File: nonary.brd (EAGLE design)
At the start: 285.8 x 82.5 mm, 145 parts, among them J1 USB-C-12401598E4#2A

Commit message: Made modifications to the keyboard.lbr, brd, and sch files
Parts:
- removed D1, D10, D11, D12, D13, D14, D15, D16, D17, D18, D19, D2, D20, D21, D22, D23, D24, D25, D26, D27, D28, D29, D3, D30, D31, D32, D33, D34, D35, D36, D37, D38, D39, D4, D40, D41, D42, D43, D44, D45, D46, D47, D48, D49, D5, D50, D51, D52, D53, D54, D55, D56, D57, D58, D59, D6, D60, D61, D62, D8, D9: (no value), Components:DFN0603-2
- removed F1, F3, F4, F5, K_", K_,, K_-, K_., K_/, K_0, K_1, K_2, K_3, K_4, K_5, K_6, K_7, K_8, K_9, K_=, K_A, K_B, K_BACKSLASH, K_BACKSPACE, K_C, K_CAPSLOCK, K_D, K_E, K_ENTER, K_F, K_G, K_H, K_I, K_J, K_K, K_L, K_LALT, K_LCTRL, K_LSHIFT, K_LWIN, K_M, K_N, K_O, K_P, K_Q, K_R, K_RALT, K_RCTRL, K_RFN1, K_RFN2, K_RSHIFT, K_RWIN, K_S, K_SEMICOLON, K_SPACE, K_T, K_TAB, K_U, K_V, K_W, K_X, K_Y, K_Z, K_[, K_], K_`: KEYSWITCH-LEDTHTHOLE-MXHS-1U-LEDTHTHOLE, Keyboard:MXHS-1U-LEDTHTHOLE
- removed J1: USB-C-12401598E4#2A, USB:12401598E4#2A
- removed R4: 22, rcl:R0603
- added C10, C11, C9: 0.1uF, Components:C0603
- added C12, C13, C14: 0.47uF, Components:C0603
- added IC1: IS31FL3733-TQLS4, SamacSys_Parts:QFP50P900X900X120-49N
- added IC2: TLV75533PDBVR, SamacSys_Parts:SOT95P280X145-5N
- added J2: USB4065-XX-X_REVA, USB4065-XX-X_REVA:GCT_USB4065-XX-X_REVA
- added K1, K2, K3, K4, K5, K6, K7, K8, K9: KEYSWITCH-RGBSMDLED-MXHSPCB-1U-SMDRGB, Keyboard:MXHSPCB-1U-SMDRGB
- added Q1, Q2: BSS138, SamacSys_Parts:SOT95P240X120-3N
- added R10, R11, R8, R9: 10K, rcl:R0603
- added R5, R6: 5.1k, rcl:R0603
- added SV1: (no value), con-lstb:MA04-1
- C8: value 22pF -> 1uF
- D7: value (none) -> PRTR5V0U2X,215; device Components:DFN0603-2 -> SamacSys_Parts:SOT-143B
- F2: value KEYSWITCH-LEDTHTHOLE-MXHS-1U-LEDTHTHOLE -> MF-PSMF020X-2; device Keyboard:MXHS-1U-LEDTHTHOLE -> SamacSys_Parts:FUSC2214X85N
- R3: value 22 -> 10K
- moved D7 364.4 mm to (23.5, 88.0), turned to 270 degrees
- moved C1 242.4 mm to (3.56, 63.6)
- moved C7 239.3 mm to (18.7, 96.8), turned to 270 degrees
- moved C2 237.7 mm to (3.56, 66.2)
- moved C3 232.9 mm to (9.40, 96.8), turned to 270 degrees
- moved U$1 229.3 mm to (21.2, 69.0), turned to 270 degrees
- moved C4 225.9 mm to (11.7, 96.8), turned to 270 degrees
- moved C8 222.3 mm to (21.1, 96.8), turned to 270 degrees
- moved C5 219.0 mm to (14.0, 96.8), turned to 270 degrees
- moved R2 217.5 mm to (29.5, 63.1)
- moved X1 215.6 mm to (9.40, 69.1), turned to 90 degrees
- moved C6 212.0 mm to (16.3, 96.8), turned to 270 degrees
- moved R1 211.1 mm to (47.1, 88.6), turned to 90 degrees
- moved S1 190.6 mm to (51.8, 95.5)
- moved R3 187.0 mm to (60.5, 78.9)
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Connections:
- net N$1 renamed XTAL1
- net N$2 renamed XTAL2
- removed net COL0: F1.MX1, F2.MX1, F3.MX1, F4.MX1, F5.MX1, U$1.36
- removed net COL1: K_CAPSLOCK.MX1, K_LCTRL.MX1, K_LSHIFT.MX1, K_TAB.MX1, K_`.MX1
- removed net COL10: K_..MX1, K_9.MX1, K_L.MX1, K_O.MX1, K_RALT.MX1
- removed net COL12: K_/.MX1, K_0.MX1, K_P.MX1, K_RWIN.MX1, K_SEMICOLON.MX1
- removed net COL13: K_".MX1, K_-.MX1, K_RFN2.MX1, K_RSHIFT.MX1, K_[.MX1
- removed net COL14: K_BACKSLASH.MX1, K_BACKSPACE.MX1, K_ENTER.MX1, K_RCTRL.MX1, K_RFN1.MX1
- removed net COL2: K_1.MX1, K_A.MX1, K_LWIN.MX1, K_Q.MX1, K_Z.MX1
- removed net COL3: K_2.MX1, K_LALT.MX1, K_S.MX1, K_W.MX1, K_X.MX1
- removed net COL4: K_3.MX1, K_C.MX1, K_D.MX1, K_E.MX1
- removed net COL5: K_4.MX1, K_F.MX1, K_R.MX1, K_V.MX1
- removed net COL6: K_5.MX1, K_B.MX1, K_G.MX1, K_SPACE.MX1, K_T.MX1
- removed net COL7: K_6.MX1, K_H.MX1, K_N.MX1, K_Y.MX1
- removed net COL8: K_7.MX1, K_J.MX1, K_M.MX1, K_U.MX1
- removed net COL9: K_,.MX1, K_8.MX1, K_I.MX1, K_K.MX1
- removed net N$10: J1.A7, J1.B7, R4.2
- removed net N$11: D1.C, D2.A, K_`.MX2
- removed net N$12: D2.C, D3.A, K_1.MX2
- removed net N$14: D4.C, D5.A, K_3.MX2
- removed net N$15: D5.C, D6.A, K_4.MX2
- removed net N$16: D6.C, D7.A, K_5.MX2
- removed net N$17: D7.C, D8.A, K_6.MX2
- removed net N$18: D8.C, D9.A, K_7.MX2
- removed net N$20: D10.C, D11.A, K_9.MX2
- removed net N$21: D11.C, D12.A, K_0.MX2
- removed net N$22: D12.C, D13.A, K_-.MX2
- removed net N$23: D28.C, K_BACKSLASH.MX2
- removed net N$24: D13.C, D14.A, K_=.MX2
- removed net N$25: D14.C, K_BACKSPACE.MX2
- removed net N$28: D17.C, D18.A, K_W.MX2
- removed net N$29: D18.C, D19.A, K_E.MX2
- removed net N$30: D19.C, D20.A, K_R.MX2
- removed net N$31: D20.C, D21.A, K_T.MX2
- removed net N$32: D21.C, D22.A, K_Y.MX2
- removed net N$33: D22.C, D23.A, K_U.MX2
- removed net N$34: D23.C, D24.A, K_I.MX2
- removed net N$35: D24.C, D25.A, K_O.MX2
- removed net N$36: D25.C, D26.A, K_P.MX2
- removed net N$37: D26.C, D27.A, K_[.MX2
- removed net N$38: D34.C, D35.A, K_G.MX2
- removed net N$39: D27.C, D28.A, K_].MX2
- removed net N$40: D41.C, K_ENTER.MX2
- removed net N$41: D29.C, D30.A, K_CAPSLOCK.MX2
- removed net N$42: D30.C, D31.A, K_A.MX2
- removed net N$43: D31.C, D32.A, K_S.MX2
- removed net N$44: D32.C, D33.A, K_D.MX2
- removed net N$45: D33.C, D34.A, K_F.MX2
- removed net N$46: D40.C, D41.A, K_".MX2
- removed net N$47: D35.C, D36.A, K_H.MX2
- removed net N$48: D36.C, D37.A, K_J.MX2
- removed net N$49: D37.C, D38.A, K_K.MX2
- removed net N$50: D38.C, D39.A, K_L.MX2
- removed net N$51: D39.C, D40.A, K_SEMICOLON.MX2
- removed net N$52: D53.C, D54.A, K_RSHIFT.MX2
- removed net N$53: D54.C, K_RFN1.MX2
- removed net N$54: D47.C, D48.A, K_B.MX2
- removed net N$55: D60.C, D61.A, K_RWIN.MX2
- removed net N$56: D42.C, D43.A, K_LSHIFT.MX2
- removed net N$57: D43.C, D44.A, K_Z.MX2
- removed net N$58: D44.C, D45.A, K_X.MX2
- removed net N$59: D45.C, D46.A, K_C.MX2
- removed net N$6: J1.A4, J1.A9, J1.B4, J1.B9, U$1.2
- removed net N$60: D46.C, D47.A, K_V.MX2
- removed net N$61: K_=.MX1, K_].MX1
- removed net N$62: D48.C, D49.A, K_N.MX2
- removed net N$63: D49.C, D50.A, K_M.MX2
- removed net N$64: D50.C, D51.A, K_,.MX2
- removed net N$65: D51.C, D52.A, K_..MX2
- removed net N$66: D52.C, D53.A, K_/.MX2
- removed net N$7: J1.A6, J1.B6, R3.1
- removed net N$71: D55.C, D56.A, K_LCTRL.MX2
- removed net N$72: D56.C, D57.A, K_LWIN.MX2
- removed net N$73: D57.C, D58.A, K_LALT.MX2
- removed net N$74: D58.C, D59.A, K_SPACE.MX2
- removed net N$75: D59.C, D60.A, K_RALT.MX2
- removed net N$77: D61.C, D62.A, K_RFN2.MX2
- removed net N$78: D62.C, K_RCTRL.MX2
- removed net N$8: R3.2, U$1.4
- removed net N$9: R4.1, U$1.3
- removed net ROW0: D1.A, F1.MX2, U$1.41
- removed net ROW1: D15.A, F2.MX2, U$1.40
- removed net ROW2: D29.A, F3.MX2, U$1.39
- removed net ROW3: D42.A, F4.MX2, U$1.38
- removed net ROW4: D55.A, F5.MX2, U$1.37
- removed net VCC: C3.2, C4.2, C5.2, C6.2, C7.2, U$1.14, U$1.24, U$1.34, U$1.44, U$1.7
- new net +5V: C3.2, C4.2, C5.2, C6.2, C7.2, F2.1, IC2.1, IC2.3, R1.1, R10.1, R8.1, SV1.3, U$1.14, U$1.2, U$1.24, U$1.34, U$1.44, U$1.7
- new net AVCC: C12.2, C9.2, IC1.37, IC1.38
- new net CS1: IC1.18, K3.LED+, K6.LED+, K9.LED+
- new net CS2: IC1.17, K2.LED+, K5.LED+, K8.LED+
- new net CS3: IC1.16, K1.LED+, K4.LED+, K7.LED+
- new net D+: D7.2, J2.A6, J2.B6, U$1.4
- new net D-: D7.3, J2.A7, J2.B7, U$1.3
- new net KEY1: K1.MX1, U$1.27
- new net KEY2: K2.MX1, U$1.38
- new net KEY3: K3.MX1, U$1.41
- new net KEY4: K4.MX1, U$1.26
- new net KEY5: K5.MX1, U$1.37
- new net KEY6: K6.MX1, U$1.40
- new net KEY7: K7.MX1, U$1.25
- new net KEY8: K8.MX1, U$1.36
- new net KEY9: K9.MX1, U$1.39
- new net PVCC_1: C11.2, C14.2, IC1.20
- new net PVCC_2: C10.2, C13.2, IC1.29
- new net SCL: Q2.3, R10.2, U$1.18
- new net SCL_3V3: IC1.42, Q2.2, R11.2, SV1.2
- new net SDA: Q1.3, R8.2, U$1.19
- new net SDA_3V3: IC1.41, Q1.2, R9.2, SV1.1
- new net SW1: IC1.2, K1.B-, K2.B-, K3.B-
- new net SW2: IC1.3, K1.G-, K2.G-, K3.G-
- new net SW3: IC1.4, K1.R-, K2.R-, K3.R-
- new net SW4: IC1.6, K4.B-, K5.B-, K6.B-
- new net SW5: IC1.7, K4.G-, K5.G-, K6.G-
- new net SW6: IC1.8, K4.R-, K5.R-, K6.R-
- new net SW7: IC1.9, K7.B-, K8.B-, K9.B-
- new net SW8: IC1.10, K7.G-, K8.G-, K9.G-
- new net SW9: IC1.11, K7.R-, K8.R-, K9.R-
- new net VBUS1.2: J2.A9
- new net VBUS2.1: J2.B4
- net +3V3: now also IC1.39, IC2.5, Q1.1, Q2.1, R11.1, R9.1; no longer R1.1
- net GND: now also C10.1, C11.1, C12.1, C13.1, C14.1, C9.1, D7.1, IC1.12, IC1.34, IC1.43, IC1.44, IC1.48, IC1.49, IC1.5, IC2.2, IC2.4, J2.1, J2.2, J2.3, J2.4, J2.A1, J2.A12, J2.B1, J2.B12, K1.MX2, K2.MX2, K3.MX2, K4.MX2, K5.MX2, K6.MX2, K7.MX2, K8.MX2, K9.MX2, R3.2, R5.2, R6.2, SV1.4; no longer J1.A1, J1.A12, J1.B1, J1.B12, J1.SHIELD@1, J1.SHIELD@2, J1.SHIELD@3, J1.SHIELD@4
- net N$13: now also J2.B5, R5.1; no longer D3.C, D4.A, K_2.MX2
- net N$19: now also J2.A5, R6.1; no longer D10.A, D9.C, K_8.MX2
- net N$26: now also IC1.35, R3.1; no longer D15.C, D16.A, K_TAB.MX2
- net N$27: now also D7.4, F2.2, J2.A4, J2.B9; no longer D16.C, D17.A, K_Q.MX2
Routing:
- net SW9: track 0.00 -> 139.3 mm, vias 0 -> 4
- net SW8: track 0.00 -> 129.5 mm, vias 0 -> 5
- net SW7: track 0.00 -> 121.1 mm, vias 0 -> 2
- net SW6: track 0.00 -> 119.9 mm, vias 0 -> 4
- net CS3: track 0.00 -> 112.8 mm, vias 0 -> 2
- net SW5: track 0.00 -> 106.1 mm, vias 0 -> 5
- net SW4: track 0.00 -> 100.4 mm, vias 0 -> 5
- net CS2: track 0.00 -> 97.8 mm, vias 0 -> 2
- net SW3: track 0.00 -> 97.6 mm, vias 0 -> 4
- net CS1: track 0.00 -> 91.3 mm
- net SW2: track 0.00 -> 88.6 mm, vias 0 -> 5
- net SW1: track 0.00 -> 84.9 mm, vias 0 -> 5
- net KEY9: track 0.00 -> 78.4 mm
- net KEY8: track 0.00 -> 74.0 mm
- net KEY7: track 0.00 -> 71.3 mm
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- added copper zone on layer 1, net GND
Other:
- board size 285.8 x 82.5 mm -> 65.9 x 100 mm

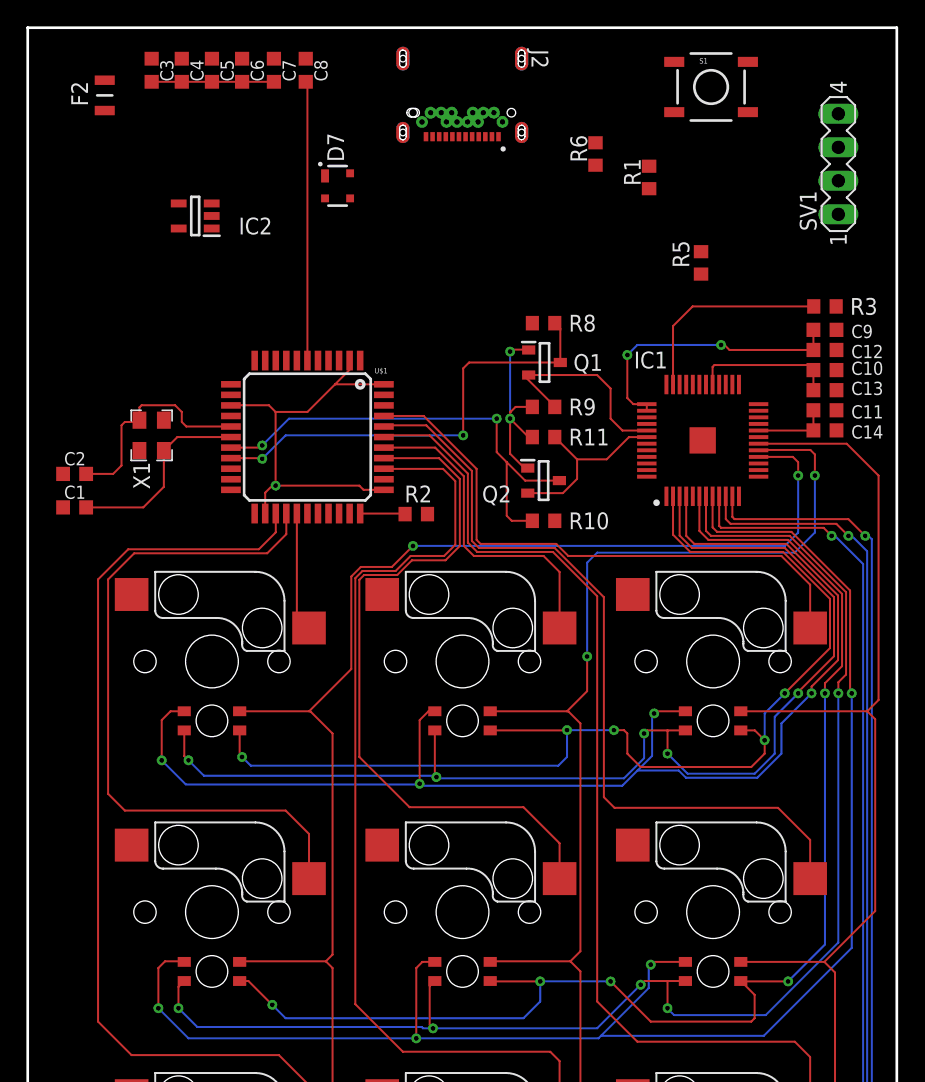
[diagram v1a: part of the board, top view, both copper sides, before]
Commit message: Routing on the Board
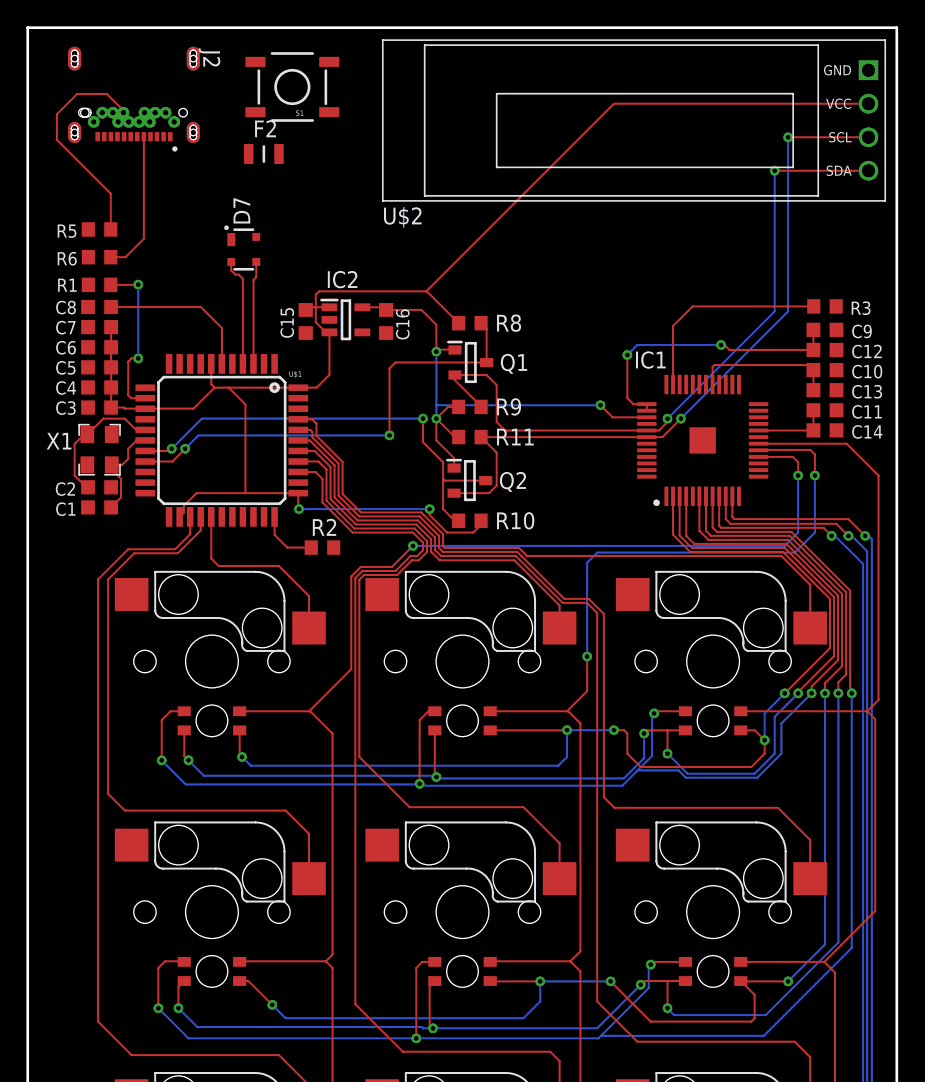
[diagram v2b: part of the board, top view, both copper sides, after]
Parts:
- removed SV1: (no value), con-lstb:MA04-1
- added C15, C16: 1uF, Components:C0603
- added U$2: DISPLAY-OLED-128X32, diy-modules:DISPLAY-OLED-128X32
- moved R5 45.7 mm to (5.45, 84.7), turned to 180 degrees
- moved R1 42.5 mm to (5.45, 80.5), turned to 0 degrees
- moved R6 38.4 mm to (5.45, 82.6), turned to 180 degrees
- moved S1 31.8 mm to (20.1, 95.5), turned to 180 degrees
- moved C3 25.9 mm to (5.45, 71.2), turned to 0 degrees
- moved J2 24.9 mm to (8.06, 95.6)
- moved C4 24.8 mm to (5.45, 72.7), turned to 0 degrees
- moved C5 24.1 mm to (5.45, 74.2), turned to 0 degrees
- moved C8 23.8 mm to (5.45, 78.8), turned to 0 degrees
- moved C6 23.6 mm to (5.45, 75.8), turned to 0 degrees
- moved C7 23.5 mm to (5.45, 77.3), turned to 0 degrees
- moved IC2 13.9 mm to (24.1, 77.9), turned to 0 degrees
- moved F2 12.9 mm to (17.9, 90.4), turned to 180 degrees
- moved D7 8.59 mm to (16.4, 83.2)
- moved R2 7.55 mm to (22.4, 60.6)
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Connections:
- net N$3 renamed /RESET
- net +3V3: now also C16.2
- net +5V: now also C15.2, U$2.2; no longer SV1.3
- net GND: now also C15.1, C16.1, U$2.1; no longer SV1.4
- net SCL_3V3: now also U$2.3; no longer SV1.2
- net SDA_3V3: now also U$2.4; no longer SV1.1
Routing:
- net +5V: track 40.7 -> 120.4 mm, vias 1 -> 2
- net SCL_3V3: track 14.2 -> 54.2 mm, vias 0 -> 2
- net SDA_3V3: track 15.8 -> 53.1 mm, vias 0 -> 2
- net +3V3: track 15.7 -> 40.3 mm, vias 2 -> 3
- net N$13: track 0.00 -> 16.8 mm
- net /RESET: track 0.00 -> 12.5 mm, vias 0 -> 2
- net N$19: track 0.00 -> 10.8 mm
- net N$5: track 21.2 -> 11.8 mm
- net D+: track 0.00 -> 8.24 mm
- net D-: track 0.00 -> 7.82 mm
- net XTAL1: track 15.0 -> 7.59 mm
- net KEY4: track 52.9 -> 46.0 mm
- net KEY7: track 71.3 -> 64.6 mm
- net KEY1: track 9.31 -> 15.7 mm
- net XTAL2: track 16.6 -> 10.3 mm
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
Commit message: New Libraries and finished board/schematic
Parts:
- removed IC2: TLV75533PDBVR, SamacSys_Parts:SOT95P280X145-5N
- removed U$2: DISPLAY-OLED-128X32, diy-modules:DISPLAY-OLED-128X32
- added C17: 1uF, Components:C0603
- added R12, R13: 100K, rcl:R0603
- added R4, R7: 4.7k, rcl:R0603
- added U2: (no value), LED:QFN-40
- added U3: DISPLAY-OLED-128X32, diy-modules:DISPLAY-OLED-128X32
- C12: value 0.47uF -> 0.1uF
- C15: value 1uF -> 0.47uF
- C9: value 0.1uF -> 0.47uF
- IC1: value IS31FL3733-TQLS4 -> TLV75533PDBVR; device SamacSys_Parts:QFP50P900X900X120-49N -> SamacSys_Parts:SOT95P280X145-5N
- J2: value USB4065-XX-X_REVA -> USB-C-12401598E4#2A; device USB4065-XX-X_REVA:GCT_USB4065-XX-X_REVA -> USB:12401598E4#2A
- R3: value 10K -> 20K
- moved C15 39.4 mm to (60.5, 77.2), turned to 180 degrees
- moved IC1 28.6 mm to (24.1, 77.9), turned to 0 degrees
- moved R3 14.8 mm to (47.8, 71.2)
- moved C9 9.02 mm to (60.5, 68.1), turned to 0 degrees
- moved C14 6.22 mm to (60.5, 75.7)
- moved C16 6.10 mm to (21.1, 77.7)
- moved J2 5.82 mm to (10.7, 90.4)
- moved D7 5.47 mm to (11.5, 85.7), turned to 0 degrees
- moved C10 4.44 mm to (60.5, 69.6)
- moved F2 4.32 mm to (21.7, 88.4)
- moved C12 2.92 mm to (60.5, 72.6)
- moved C13 1.65 mm to (60.5, 74.2)
- moved S1 1.30 mm to (20.3, 94.2)
- moved C11 0.13 mm to (60.5, 71.1)
- renumbered U$1 to U1
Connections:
- removed net AVCC: C12.2, C9.2, IC1.37, IC1.38
- removed net N$26: IC1.35, R3.1
- removed net PVCC_1: C11.2, C14.2, IC1.20
- removed net PVCC_2: C10.2, C13.2, IC1.29
- removed net VBUS1.2: J2.A9
- removed net VBUS2.1: J2.B4
- new net N$1: R12.1, U2.39
- new net N$2: R3.1, U2.30
- new net SDB: R13.1, U1.1, U2.38
- net +3V3: now also C17.2, C9.1, IC1.5, R4.1, R7.1, U2.32; no longer C16.2, IC1.39, IC2.5
- net +5V: now also C10.2, C11.2, C12.2, C13.2, C14.2, C16.2, IC1.1, IC1.3, U1.42, U2.19, U2.26, U2.31, U3.2; no longer IC2.1, IC2.3, U$2.2
- net CS1: now also U2.15; no longer IC1.18
- net CS2: now also U2.16; no longer IC1.17
- net CS3: now also U2.17; no longer IC1.16
- net GND: now also C17.1, C9.2, IC1.2, J2.SHIELD@1, J2.SHIELD@2, J2.SHIELD@3, J2.SHIELD@4, R12.2, R13.2, U2.11, U2.29, U2.36, U2.4, U2.40, U2.TAB, U3.1; no longer C9.1, IC1.12, IC1.34, IC1.43, IC1.44, IC1.48, IC1.49, IC1.5, IC2.2, IC2.4, J2.1, J2.2, J2.3, J2.4, U$2.1
- net N$27: now also J2.A9, J2.B4
- net SCL_3V3: now also R7.2, U2.35, U3.3; no longer IC1.42, U$2.3
- net SDA_3V3: now also R4.2, U2.34, U3.4; no longer IC1.41, U$2.4
- net SW1: now also U2.1; no longer IC1.2
- net SW2: now also U2.2; no longer IC1.3
- net SW3: now also U2.3; no longer IC1.4
- net SW4: now also U2.5; no longer IC1.6
- net SW5: now also U2.6; no longer IC1.7
- net SW6: now also U2.7; no longer IC1.8
- net SW7: now also U2.8; no longer IC1.9
- net SW8: now also U2.9; no longer IC1.10
- net SW9: now also U2.10; no longer IC1.11
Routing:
- net GND: track 1.02 -> 472.5 mm, vias 0 -> 28
- net +5V: track 120.4 -> 28.2 mm, vias 2 -> 0
- net SDB: track 0.00 -> 37.9 mm, vias 0 -> 4
- net /RESET: track 12.5 -> 37.7 mm, vias 2 -> 5
- net +3V3: track 40.3 -> 63.3 mm, vias 3 -> 5
- net N$27: track 0.00 -> 22.6 mm, vias 0 -> 2
- net AVCC: track 21.9 -> 0.00 mm, vias 2 -> 0
- net D-: track 7.82 -> 28.9 mm, vias 0 -> 4
- net N$26: track 15.7 -> 0.00 mm
- net D+: track 8.24 -> 20.2 mm, vias 0 -> 2
- net SCL_3V3: track 54.2 -> 66.1 mm, vias 2 -> 3
- net PVCC_2: track 10.7 -> 0.00 mm
- net N$2: track 0.00 -> 7.91 mm, vias 0 -> 2
- net SDA_3V3: track 53.1 -> 60.9 mm
- net CS3: track 112.8 -> 120.5 mm
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- added copper zone on layer 1, net +5V
- added copper zone on layer 16, net GND
- removed copper zone on layer 1, net GND
